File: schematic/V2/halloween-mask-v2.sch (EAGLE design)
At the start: 21 parts, among them J1 EL-Wire-Inverter, J5 PIR, Q1 IRLB8721PBF, U1 MCP1826T-3302E_DC, U2 Adafruit-ITSY-BITSY-M0

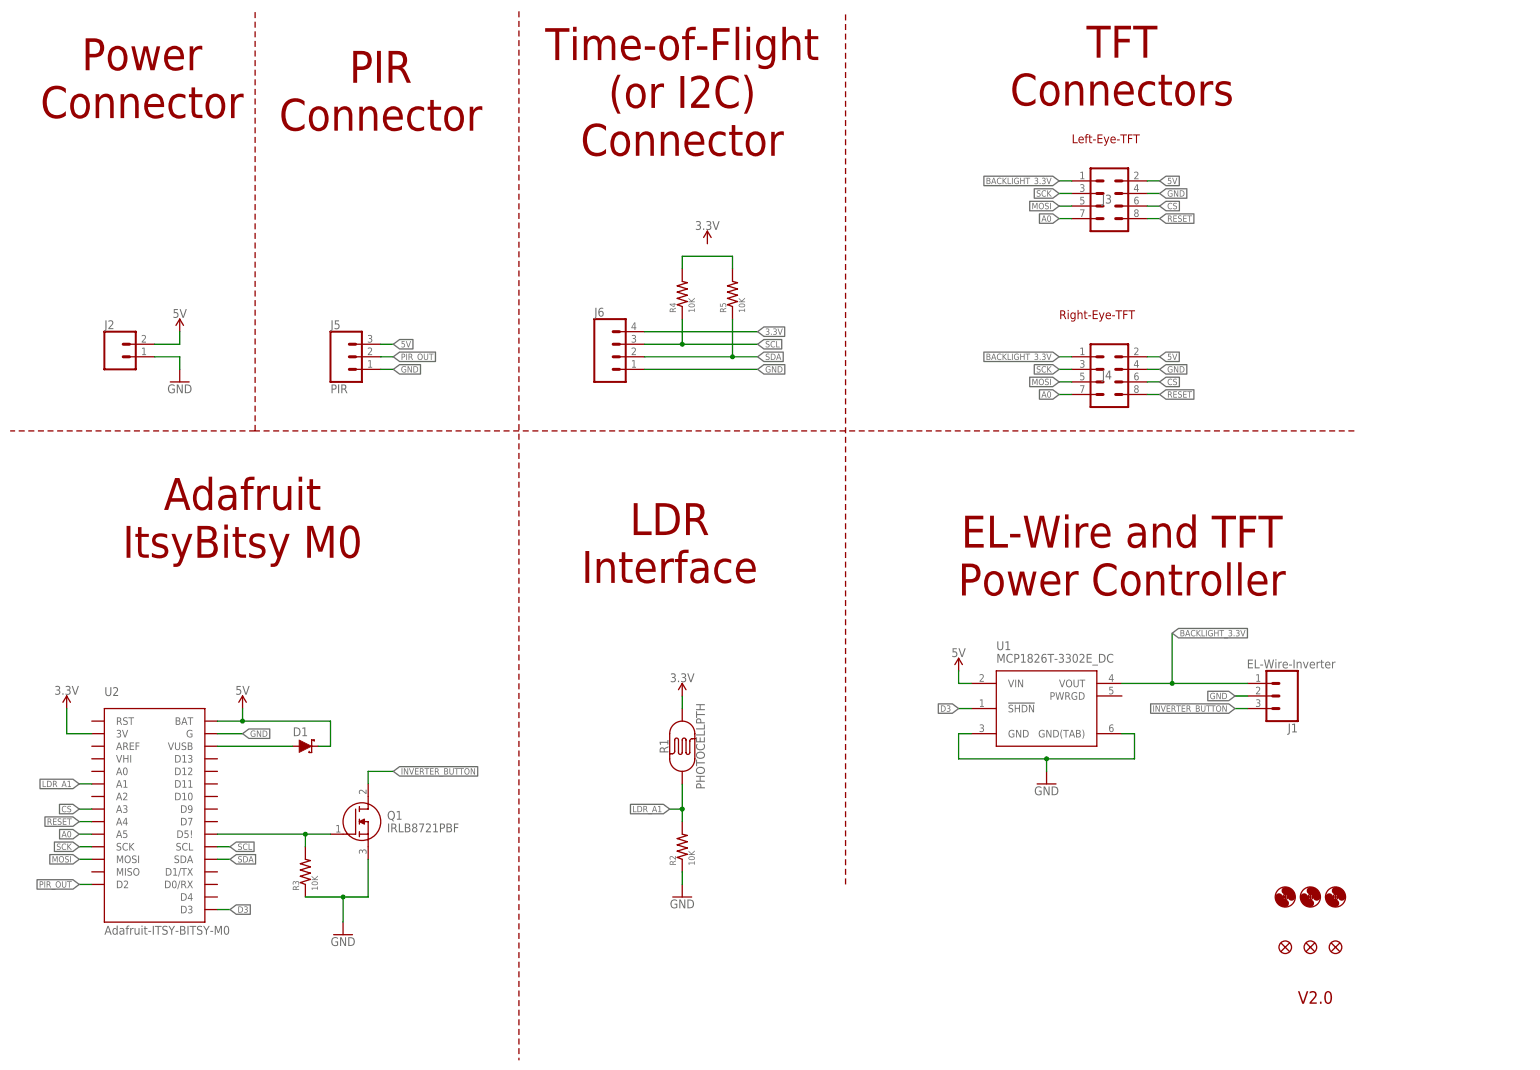
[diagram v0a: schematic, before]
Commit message: Added a connector for ToF. Added a schotky diode from Vusb to Vbat, so that I can both use external power and USB.
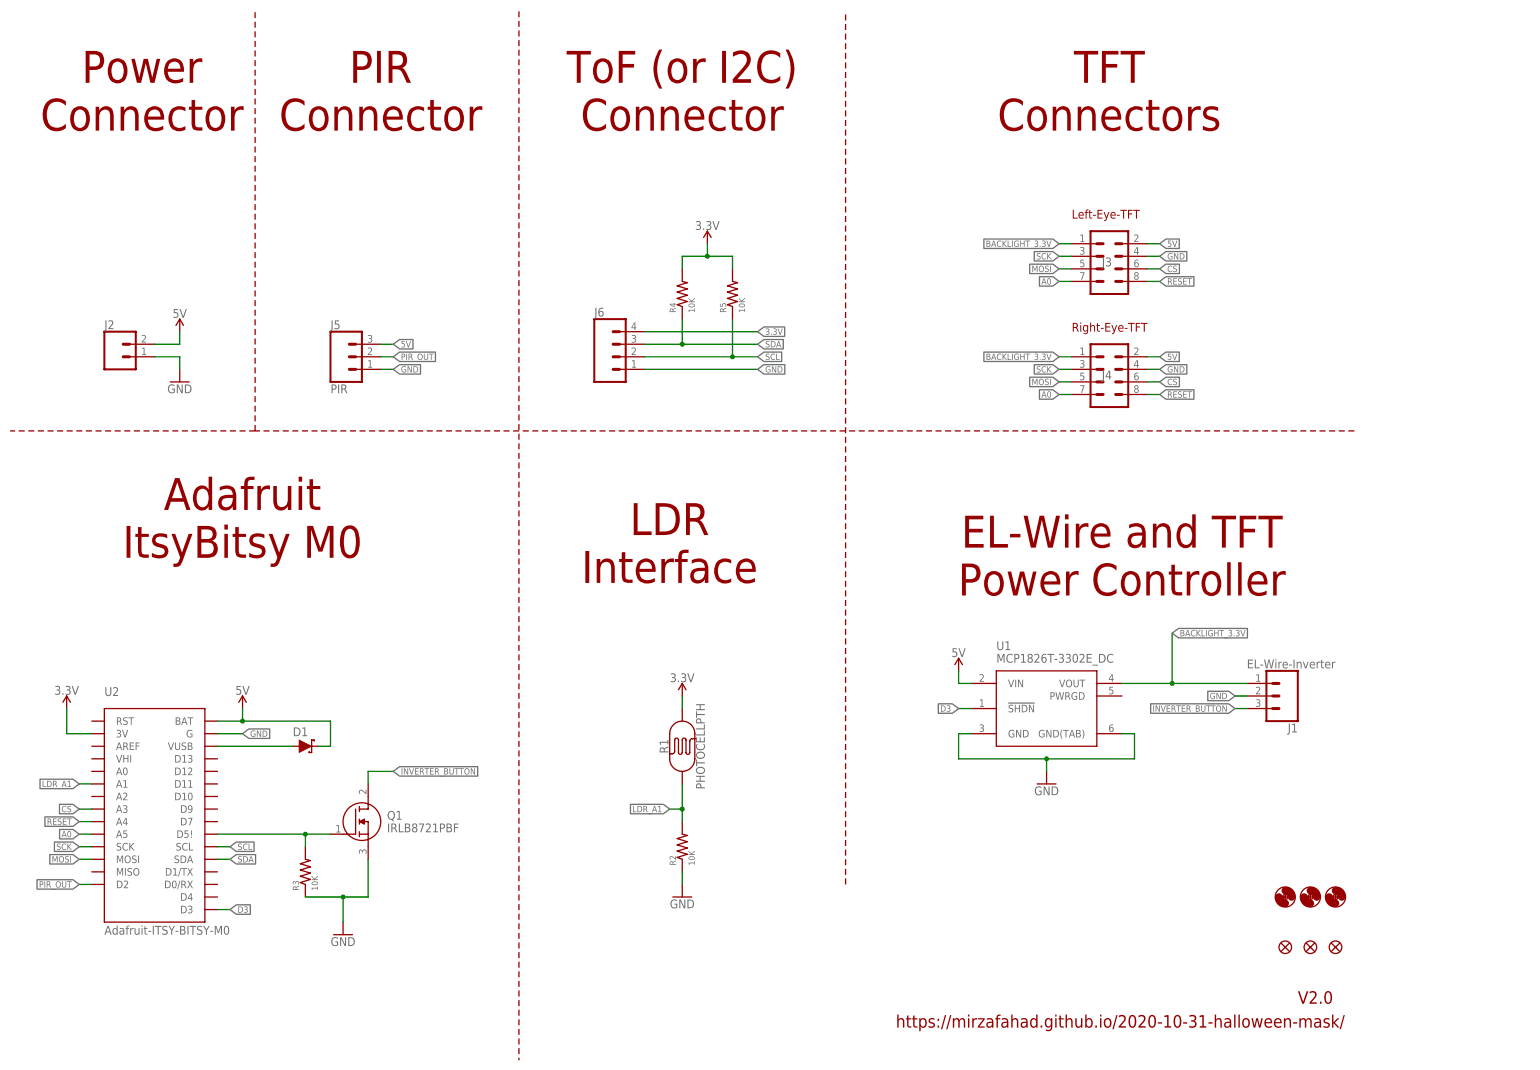
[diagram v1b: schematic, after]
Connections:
- removed net N$9: R4.2, R5.2
- net 3.3V: now also R4.2, R5.2
- net SCL: now also J6.2, R5.1; no longer J6.3, R4.1
- net SDA: now also J6.3, R4.1; no longer J6.2, R5.1
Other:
- note added: "ToF (or I2C) Connector"
- note added: "https://mirzafahad.github.io/2020-10-31-halloween-mask/"
- note removed: "Time-of-Flight (or I2C) Connector"
- moved on the sheet: J3
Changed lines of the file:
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@@
 <plain>
 <text x="264.16" y="11.43" size="2.54" layer="94" ratio="12">V2.0</text>
-<text x="228.6" y="193.04" size="6.4516" layer="94" font="vector" ratio="12" align="bottom-center">TFT
+<text x="226.06" y="187.96" size="6.4516" layer="94" font="vector" ratio="12" align="bottom-center">TFT
 Connectors</text>
-<text x="218.44" y="185.42" size="1.778" layer="94" font="vector" ratio="12">Left-Eye-TFT</text>
-<text x="215.9" y="149.86" size="1.778" layer="94" font="vector" ratio="12">Right-Eye-TFT</text>
-<text x="139.7" y="182.88" size="6.4516" layer="94" font="vector" ratio="12" align="bottom-center">Time-of-Flight
-(or I2C)
+<text x="218.44" y="170.18" size="1.778" layer="94" font="vector" ratio="12">Left-Eye-TFT</text>
+<text x="218.44" y="147.32" size="1.778" layer="94" font="vector" ratio="12">Right-Eye-TFT</text>
+<text x="139.7" y="187.96" size="6.4516" layer="94" font="vector" ratio="12" align="bottom-center">ToF (or I2C)
 Connector</text>
 <text x="228.6" y="93.98" size="6.4516" layer="94" font="vector" ratio="12" align="bottom-center">EL-Wire and TFT
@@
 <text x="78.74" y="187.96" size="6.4516" layer="94" font="vector" ratio="12" align="bottom-center">PIR
 Connector</text>
-<text x="30.48" y="190.5" size="6.4516" layer="94" font="vector" ratio="12" align="bottom-center">Power
+<text x="30.48" y="187.96" size="6.4516" layer="94" font="vector" ratio="12" align="bottom-center">Power
 Connector</text>
 <wire x1="172.72" y1="35.56" x2="172.72" y2="212.09" width="0.1" layer="94" style="shortdash"/>
@@
 <text x="50.8" y="101.6" size="6.4516" layer="94" font="vector" ratio="12" align="bottom-center">Adafruit
 ItsyBitsy M0</text>
+<text x="182.88" y="6.604" size="2.54" layer="94">https://mirzafahad.github.io/2020-10-31-halloween-mask/</text>
 </plain>
 <instances>
@@
 <attribute name="VALUE" x="71.12" y="23.114" size="1.778" layer="96" rot="R180" align="top-center"/>
 </instance>
-<instance part="J3" gate="G$1" x="226.06" y="172.72" smashed="yes">
-<attribute name="VALUE" x="222.25" y="165.354" size="1.778" layer="96" font="vector"/>
-<attribute name="NAME" x="224.536" y="173.228" size="1.778" layer="95" font="vector"/>
+<instance part="J3" gate="G$1" x="226.06" y="160.02" smashed="yes">
+<attribute name="VALUE" x="222.25" y="152.654" size="1.778" layer="96" font="vector"/>
+<attribute name="NAME" x="224.536" y="160.528" size="1.778" layer="95" font="vector"/>
 </instance>
 <instance part="J4" gate="G$1" x="226.06" y="137.16" smashed="yes">
@@
 <segment>
 <pinref part="J3" gate="G$1" pin="4"/>
-<wire x1="233.68" y1="175.26" x2="236.22" y2="175.26" width="0.1524" layer="91"/>
-<label x="236.22" y="175.26" size="1.27" layer="95" xref="yes"/>
+<wire x1="233.68" y1="162.56" x2="236.22" y2="162.56" width="0.1524" layer="91"/>
+<label x="236.22" y="162.56" size="1.27" layer="95" xref="yes"/>
 </segment>
 <segment>
@@
 <segment>
 <pinref part="J3" gate="G$1" pin="2"/>
-<wire x1="233.68" y1="177.8" x2="236.22" y2="177.8" width="0.1524" layer="91"/>
-<label x="236.22" y="177.8" size="1.27" layer="95" xref="yes"/>
+<wire x1="233.68" y1="165.1" x2="236.22" y2="165.1" width="0.1524" layer="91"/>
+<label x="236.22" y="165.1" size="1.27" layer="95" xref="yes"/>
 </segment>
 <segment>
@@
 <segment>
 <pinref part="J3" gate="G$1" pin="6"/>
-<wire x1="233.68" y1="172.72" x2="236.22" y2="172.72" width="0.1524" layer="91"/>
-<label x="236.22" y="172.72" size="1.27" layer="95" xref="yes"/>
+<wire x1="233.68" y1="160.02" x2="236.22" y2="160.02" width="0.1524" layer="91"/>
+<label x="236.22" y="160.02" size="1.27" layer="95" xref="yes"/>
 </segment>
 <segment>
@@
 <segment>
 <pinref part="J3" gate="G$1" pin="8"/>
-<wire x1="233.68" y1="170.18" x2="236.22" y2="170.18" width="0.1524" layer="91"/>
-<label x="236.22" y="170.18" size="1.27" layer="95" xref="yes"/>
+<wire x1="233.68" y1="157.48" x2="236.22" y2="157.48" width="0.1524" layer="91"/>
+<label x="236.22" y="157.48" size="1.27" layer="95" xref="yes"/>
 </segment>
 <segment>
@@
 <segment>
 <pinref part="J3" gate="G$1" pin="7"/>
-<wire x1="218.44" y1="170.18" x2="215.9" y2="170.18" width="0.1524" layer="91"/>
-<label x="215.9" y="170.18" size="1.27" layer="95" rot="R180" xref="yes"/>
+<wire x1="218.44" y1="157.48" x2="215.9" y2="157.48" width="0.1524" layer="91"/>
+<label x="215.9" y="157.48" size="1.27" layer="95" rot="R180" xref="yes"/>
 </segment>
 <segment>
@@
 <segment>
 <pinref part="J3" gate="G$1" pin="3"/>
-<wire x1="218.44" y1="175.26" x2="215.9" y2="175.26" width="0.1524" layer="91"/>
-<label x="215.9" y="175.26" size="1.27" layer="95" rot="R180" xref="yes"/>
+<wire x1="218.44" y1="162.56" x2="215.9" y2="162.56" width="0.1524" layer="91"/>
+<label x="215.9" y="162.56" size="1.27" layer="95" rot="R180" xref="yes"/>
 </segment>
 <segment>
@@
 <segment>
 <pinref part="J3" gate="G$1" pin="5"/>
-<wire x1="218.44" y1="172.72" x2="215.9" y2="172.72" width="0.1524" layer="91"/>
-<label x="215.9" y="172.72" size="1.27" layer="95" rot="R180" xref="yes"/>
+<wire x1="218.44" y1="160.02" x2="215.9" y2="160.02" width="0.1524" layer="91"/>
+<label x="215.9" y="160.02" size="1.27" layer="95" rot="R180" xref="yes"/>
 </segment>
 <segment>
@@
 <wire x1="132.08" y1="147.32" x2="154.94" y2="147.32" width="0.1524" layer="91"/>
 <label x="154.94" y="147.32" size="1.27" layer="95" font="vector" ratio="12" xref="yes"/>
+</segment>
+<segment>
+<pinref part="R4" gate="R1" pin="2"/>
+<wire x1="139.7" y1="160.02" x2="139.7" y2="162.56" width="0.1524" layer="91"/>
+<wire x1="139.7" y1="162.56" x2="144.78" y2="162.56" width="0.1524" layer="91"/>
+<pinref part="R5" gate="R1" pin="2"/>
+<wire x1="144.78" y1="162.56" x2="149.86" y2="162.56" width="0.1524" layer="91"/>
+<wire x1="149.86" y1="162.56" x2="149.86" y2="160.02" width="0.1524" layer="91"/>
+<pinref part="SUPPLY6" gate="G$1" pin="3.3V"/>
+<wire x1="144.78" y1="165.1" x2="144.78" y2="162.56" width="0.1524" layer="91"/>
+<junction x="144.78" y="162.56"/>
 </segment>
 </net>
@@
 <segment>
 <pinref part="J3" gate="G$1" pin="1"/>
-<wire x1="218.44" y1="177.8" x2="215.9" y2="177.8" width="0.1524" layer="91"/>
-<label x="215.9" y="177.8" size="1.27" layer="95" font="vector" ratio="12" rot="R180" xref="yes"/>
+<wire x1="218.44" y1="165.1" x2="215.9" y2="165.1" width="0.1524" layer="91"/>
+<label x="215.9" y="165.1" size="1.27" layer="95" font="vector" ratio="12" rot="R180" xref="yes"/>
 </segment>
 <segment>
@@
 <net name="SDA" class="0">
 <segment>
+<pinref part="U2" gate="U1" pin="SDA"/>
+<wire x1="45.72" y1="40.64" x2="48.26" y2="40.64" width="0.1524" layer="91"/>
+<label x="48.26" y="40.64" size="1.27" layer="95" font="vector" ratio="12" xref="yes"/>
+</segment>
+<segment>
+<pinref part="J6" gate="J1" pin="3"/>
+<pinref part="R4" gate="R1" pin="1"/>
+<wire x1="139.7" y1="149.86" x2="139.7" y2="144.78" width="0.1524" layer="91"/>
+<wire x1="139.7" y1="144.78" x2="132.08" y2="144.78" width="0.1524" layer="91"/>
+<wire x1="139.7" y1="144.78" x2="154.94" y2="144.78" width="0.1524" layer="91"/>
+<junction x="139.7" y="144.78"/>
+<label x="154.94" y="144.78" size="1.27" layer="95" font="vector" ratio="12" xref="yes"/>
+</segment>
+</net>
+<net name="SCL" class="0">
+<segment>
+<pinref part="U2" gate="U1" pin="SCL"/>
+<wire x1="45.72" y1="43.18" x2="48.26" y2="43.18" width="0.1524" layer="91"/>
+<label x="48.26" y="43.18" size="1.27" layer="95" font="vector" ratio="12" xref="yes"/>
+</segment>
+<segment>
 <pinref part="J6" gate="J1" pin="2"/>
 <wire x1="132.08" y1="142.24" x2="149.86" y2="142.24" width="0.1524" layer="91"/>
@@
 <label x="154.94" y="142.24" size="1.27" layer="95" font="vector" ratio="12" xref="yes"/>
 </segment>
-<segment>
-<pinref part="U2" gate="U1" pin="SDA"/>
-<wire x1="45.72" y1="40.64" x2="48.26" y2="40.64" width="0.1524" layer="91"/>
-<label x="48.26" y="40.64" size="1.27" layer="95" font="vector" ratio="12" xref="yes"/>
-</segment>
-</net>
-<net name="SCL" class="0">
-<segment>
-<pinref part="J6" gate="J1" pin="3"/>
-<pinref part="R4" gate="R1" pin="1"/>
-<wire x1="139.7" y1="149.86" x2="139.7" y2="144.78" width="0.1524" layer="91"/>
-<wire x1="139.7" y1="144.78" x2="132.08" y2="144.78" width="0.1524" layer="91"/>
-<wire x1="139.7" y1="144.78" x2="154.94" y2="144.78" width="0.1524" layer="91"/>
-<junction x="139.7" y="144.78"/>
-<label x="154.94" y="144.78" size="1.27" layer="95" font="vector" ratio="12" xref="yes"/>
-</segment>
-<segment>
-<pinref part="U2" gate="U1" pin="SCL"/>
-<wire x1="45.72" y1="43.18" x2="48.26" y2="43.18" width="0.1524" layer="91"/>
-<label x="48.26" y="43.18" size="1.27" layer="95" font="vector" ratio="12" xref="yes"/>
-</segment>
-</net>
-<net name="N$9" class="0">
-<segment>
-<pinref part="R4" gate="R1" pin="2"/>
-<wire x1="139.7" y1="160.02" x2="139.7" y2="162.56" width="0.1524" layer="91"/>
-<wire x1="139.7" y1="162.56" x2="149.86" y2="162.56" width="0.1524" layer="91"/>
-<pinref part="R5" gate="R1" pin="2"/>
-<wire x1="149.86" y1="162.56" x2="149.86" y2="160.02" width="0.1524" layer="91"/>
-</segment>
-</net>
+</net>
